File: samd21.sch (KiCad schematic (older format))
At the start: 17 parts, among them IC1 SAMD21G18A, J1 USB_C, J2 DEBUG, SW1 RESET, U4 GD25Q32C

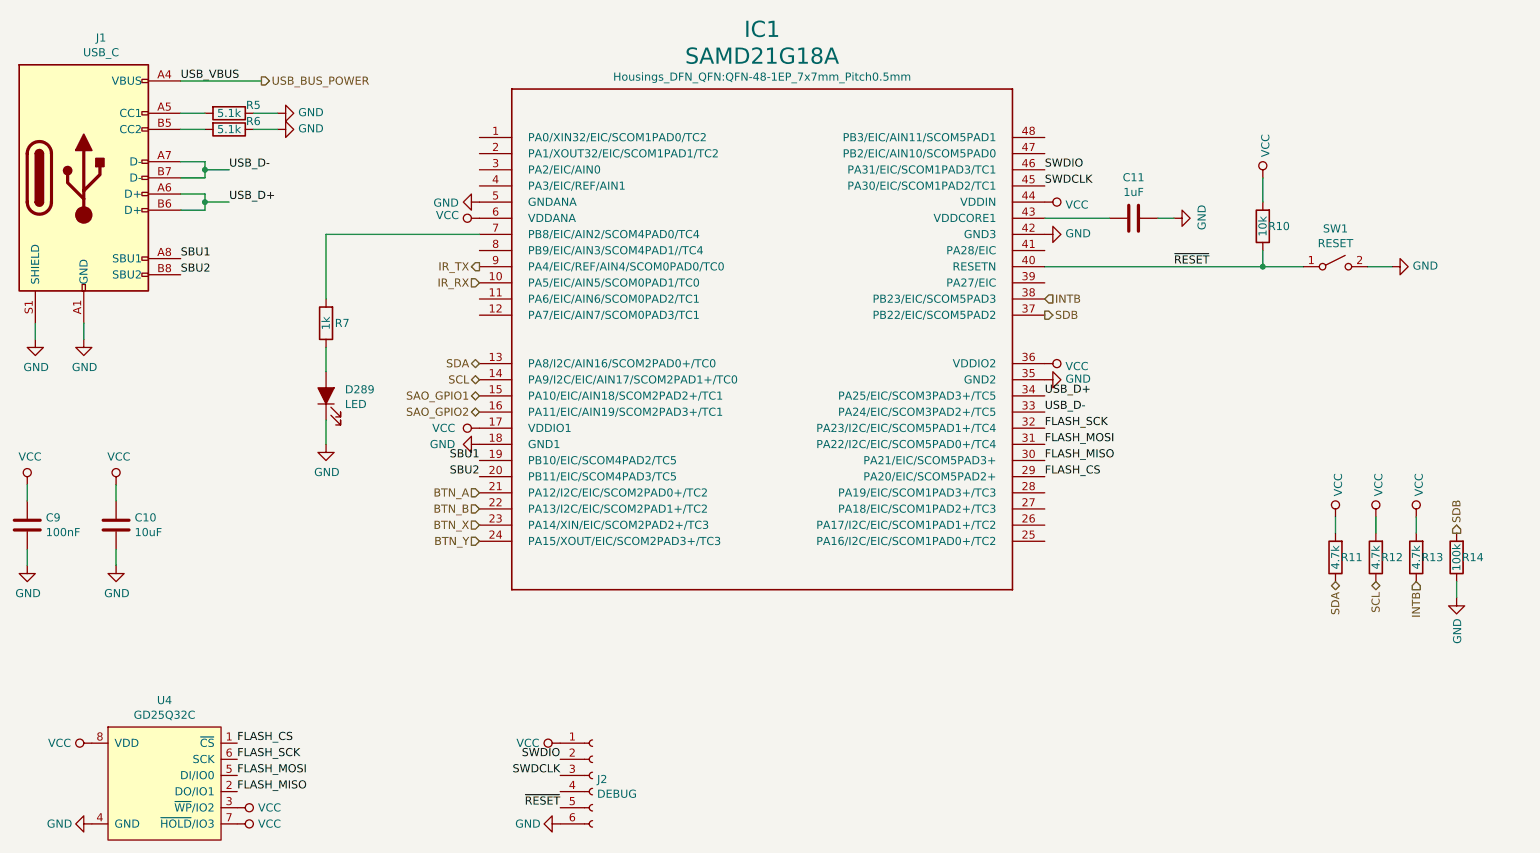
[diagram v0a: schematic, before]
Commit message: Updates to production version
Changed infrared setup, added step-up for battery power, added battery power switch, added more capacitors, changed and added logos, etc.
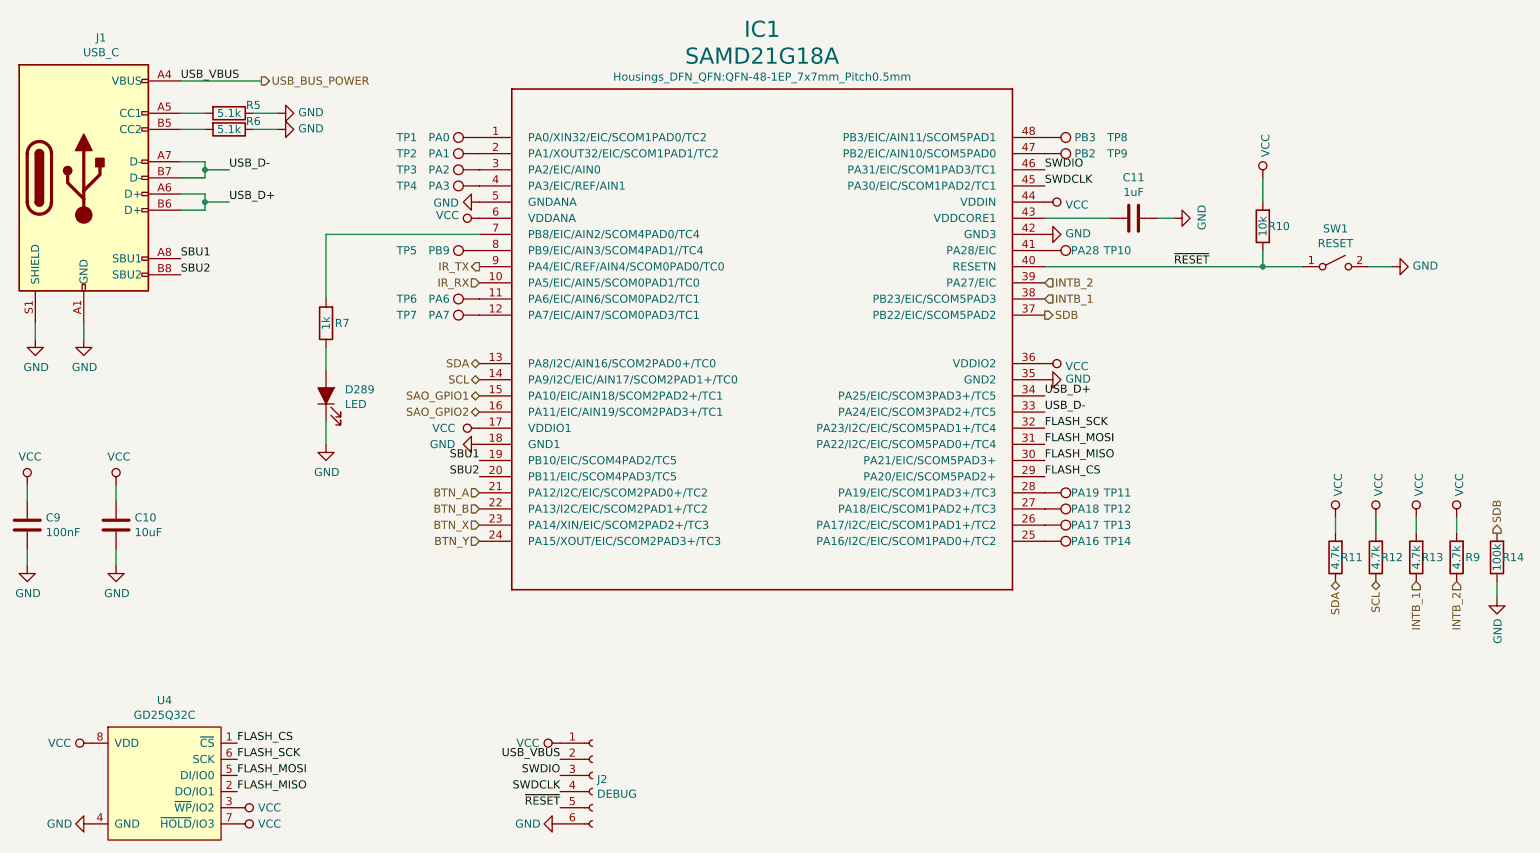
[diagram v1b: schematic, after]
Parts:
- added R9: 4.7k, Resistors_SMD:R_0603, symbol device:R
- added TP1: PA0, Connectors:TestPoint_Large, symbol Connector:TestPoint
- added TP10: PA28, Connectors:TestPoint_Large, symbol Connector:TestPoint
- added TP11: PA19, Connectors:TestPoint_Large, symbol Connector:TestPoint
- added TP12: PA18, Connectors:TestPoint_Large, symbol Connector:TestPoint
- added TP13: PA17, Connectors:TestPoint_Large, symbol Connector:TestPoint
- added TP14: PA16, Connectors:TestPoint_Large, symbol Connector:TestPoint
- added TP2: PA1, Connectors:TestPoint_Large, symbol Connector:TestPoint
- added TP3: PA2, Connectors:TestPoint_Large, symbol Connector:TestPoint
- added TP4: PA3, Connectors:TestPoint_Large, symbol Connector:TestPoint
- added TP5: PB9, Connectors:TestPoint_Large, symbol Connector:TestPoint
- added TP6: PA6, Connectors:TestPoint_Large, symbol Connector:TestPoint
- added TP7: PA7, Connectors:TestPoint_Large, symbol Connector:TestPoint
- added TP8: PB3, Connectors:TestPoint_Large, symbol Connector:TestPoint
- added TP9: PB2, Connectors:TestPoint_Large, symbol Connector:TestPoint
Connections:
- net SWDCLK: now also J2.4 (Pin_4); no longer J2.3 (Pin_3)
- net SWDIO: now also J2.3 (Pin_3); no longer J2.2 (Pin_2)
- net USB_BUS_POWER: now also J2.2 (Pin_2)
- net VCC: now also R9.2
- net at IC1.1 (PA0/XIN32/EIC/SCOM1PAD0/TC2): now also TP1.1
- net at IC1.11 (PA6/EIC/AIN6/SCOM0PAD2/TC1): now also TP6.1
- net at IC1.12 (PA7/EIC/AIN7/SCOM0PAD3/TC1): now also TP7.1
- net at IC1.2 (PA1/XOUT32/EIC/SCOM1PAD1/TC2): now also TP2.1
- net at IC1.25 (PA16/I2C/EIC/SCOM1PAD0+/TC2): now also TP14.1
- net at IC1.26 (PA17/I2C/EIC/SCOM1PAD1+/TC2): now also TP13.1
- net at IC1.27 (PA18/EIC/SCOM1PAD2+/TC3): now also TP12.1
- net at IC1.28 (PA19/EIC/SCOM1PAD3+/TC3): now also TP11.1
- net at IC1.3 (PA2/EIC/AIN0): now also TP3.1
- net INTB_2: now reaches IC1.39 (PA27/EIC)
- net INTB_2: now also R9.1
- net at IC1.4 (PA3/EIC/REF/AIN1): now also TP4.1
- net at IC1.41 (PA28/EIC): now also TP10.1
- net at IC1.47 (PB2/EIC/AIN10/SCOM5PAD0): now also TP9.1
- net at IC1.48 (PB3/EIC/AIN11/SCOM5PAD1): now also TP8.1
- net at IC1.8 (PB9/EIC/AIN3/SCOM4PAD1//TC4): now also TP5.1
- net INTB renamed INTB_1
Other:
- moved on the sheet: R14
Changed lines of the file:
@@
 Text Label 4450 5900 2    50   ~ 0
 ~RESET
-Text Label 4450 5600 2    50   ~ 0
+Text Label 4450 5700 2    50   ~ 0
 SWDIO
-Text Label 4450 5700 2    50   ~ 0
+Text Label 4450 5800 2    50   ~ 0
 SWDCLK
 Text HLabel 3950 3150 0    50   BiDi ~ 0
@@
 $EndComp
 $Comp
-L power:VCC #PWR?
+L power:VCC #PWR067
 U 1 1 5EEE4255
 P 9250 4100
-F 0 "#PWR?" H 9250 3950 50  0001 C CNN
+F 0 "#PWR067" H 9250 3950 50  0001 C CNN
 F 1 "VCC" V 9267 4228 50  0000 L CNN
 F 2 "" H 9250 4100 50  0001 C CNN
@@
 $EndComp
 $Comp
-L power:VCC #PWR?
+L power:VCC #PWR068
 U 1 1 5EEE4871
 P 9500 4100
-F 0 "#PWR?" H 9500 3950 50  0001 C CNN
+F 0 "#PWR068" H 9500 3950 50  0001 C CNN
 F 1 "VCC" V 9517 4228 50  0000 L CNN
 F 2 "" H 9500 4100 50  0001 C CNN
@@
 $EndComp
 $Comp
-L power:VCC #PWR?
+L power:VCC #PWR069
 U 1 1 5EEE49E0
 P 9750 4100
-F 0 "#PWR?" H 9750 3950 50  0001 C CNN
+F 0 "#PWR069" H 9750 3950 50  0001 C CNN
 F 1 "VCC" V 9767 4228 50  0000 L CNN
 F 2 "" H 9750 4100 50  0001 C CNN
@@
 SCL
 Text HLabel 7450 2750 2    50   Input ~ 0
-INTB
-Text HLabel 9750 4500 3    50   Input ~ 0
-INTB
+INTB_1
 Text HLabel 7450 2850 2    50   Output ~ 0
 SDB
@@
 L device:R R14
 U 1 1 5EEEA025
+P 10250 4350
+F 0 "R14" H 10150 4350 50  0000 C CNN
+F 1 "100k" V 10250 4350 50  0000 C CNN
+F 2 "Resistors_SMD:R_0603" V 10180 4350 50  0001 C CNN
+F 3 "~" H 10250 4350 50  0001 C CNN
+	1    10250 4350
+	-1   0    0    1
+$EndComp
+Text HLabel 10250 4200 1    50   Output ~ 0
+SDB
+$Comp
+L power:GND #PWR071
+U 1 1 5EEEA48A
+P 10250 4600
+F 0 "#PWR071" H 10250 4350 50  0001 C CNN
+F 1 "GND" V 10255 4472 50  0000 R CNN
+F 2 "" H 10250 4600 50  0001 C CNN
+F 3 "" H 10250 4600 50  0001 C CNN
+	1    10250 4600
+	1    0    0    -1
+$EndComp
+Wire Wire Line
+	10250 4500 10250 4600
+$Comp
+L Connector:TestPoint TP1
+U 1 1 5F12438C
+P 3950 1750
+F 0 "TP1" V 3950 2200 50  0000 C CNN
+F 1 "PA0" V 3950 2000 50  0000 C CNN
+F 2 "Connectors:TestPoint_Large" H 4150 1750 50  0001 C CNN
+F 3 "~" H 4150 1750 50  0001 C CNN
+	1    3950 1750
+	0    -1   -1   0
+$EndComp
+$Comp
+L Connector:TestPoint TP2
+U 1 1 5F125D74
+P 3950 1850
+F 0 "TP2" V 3950 2300 50  0000 C CNN
+F 1 "PA1" V 3950 2100 50  0000 C CNN
+F 2 "Connectors:TestPoint_Large" H 4150 1850 50  0001 C CNN
+F 3 "~" H 4150 1850 50  0001 C CNN
+	1    3950 1850
+	0    -1   -1   0
+$EndComp
+$Comp
+L Connector:TestPoint TP3
+U 1 1 5F12663A
+P 3950 1950
+F 0 "TP3" V 3950 2400 50  0000 C CNN
+F 1 "PA2" V 3950 2200 50  0000 C CNN
+F 2 "Connectors:TestPoint_Large" H 4150 1950 50  0001 C CNN
+F 3 "~" H 4150 1950 50  0001 C CNN
+	1    3950 1950
+	0    -1   -1   0
+$EndComp
+$Comp
+L Connector:TestPoint TP4
+U 1 1 5F126A64
+P 3950 2050
+F 0 "TP4" V 3950 2500 50  0000 C CNN
+F 1 "PA3" V 3950 2300 50  0000 C CNN
+F 2 "Connectors:TestPoint_Large" H 4150 2050 50  0001 C CNN
+F 3 "~" H 4150 2050 50  0001 C CNN
+	1    3950 2050
+	0    -1   -1   0
+$EndComp
+$Comp
+L Connector:TestPoint TP5
+U 1 1 5F127893
+P 3950 2450
+F 0 "TP5" V 3950 2900 50  0000 C CNN
+F 1 "PB9" V 3950 2700 50  0000 C CNN
+F 2 "Connectors:TestPoint_Large" H 4150 2450 50  0001 C CNN
+F 3 "~" H 4150 2450 50  0001 C CNN
+	1    3950 2450
+	0    -1   -1   0
+$EndComp
+$Comp
+L Connector:TestPoint TP6
+U 1 1 5F127DA0
+P 3950 2750
+F 0 "TP6" V 3950 3200 50  0000 C CNN
+F 1 "PA6" V 3950 3000 50  0000 C CNN
+F 2 "Connectors:TestPoint_Large" H 4150 2750 50  0001 C CNN
+F 3 "~" H 4150 2750 50  0001 C CNN
+	1    3950 2750
+	0    -1   -1   0
+$EndComp
+$Comp
+L Connector:TestPoint TP7
+U 1 1 5F128145
+P 3950 2850
+F 0 "TP7" V 3950 3300 50  0000 C CNN
+F 1 "PA7" V 3950 3100 50  0000 C CNN
+F 2 "Connectors:TestPoint_Large" H 4150 2850 50  0001 C CNN
+F 3 "~" H 4150 2850 50  0001 C CNN
+	1    3950 2850
+	0    -1   -1   0
+$EndComp
+$Comp
+L Connector:TestPoint TP14
+U 1 1 5F128571
+P 7450 4250
+F 0 "TP14" V 7450 4700 50  0000 C CNN
+F 1 "PA16" V 7450 4500 50  0000 C CNN
+F 2 "Connectors:TestPoint_Large" H 7650 4250 50  0001 C CNN
+F 3 "~" H 7650 4250 50  0001 C CNN
+	1    7450 4250
+	0    1    1    0
+$EndComp
+$Comp
+L Connector:TestPoint TP13
+U 1 1 5F1299EA
+P 7450 4150
+F 0 "TP13" V 7450 4600 50  0000 C CNN
+F 1 "PA17" V 7450 4400 50  0000 C CNN
+F 2 "Connectors:TestPoint_Large" H 7650 4150 50  0001 C CNN
+F 3 "~" H 7650 4150 50  0001 C CNN
+	1    7450 4150
+	0    1    1    0
+$EndComp
+$Comp
+L Connector:TestPoint TP12
+U 1 1 5F12A0AD
+P 7450 4050
+F 0 "TP12" V 7450 4500 50  0000 C CNN
+F 1 "PA18" V 7450 4300 50  0000 C CNN
+F 2 "Connectors:TestPoint_Large" H 7650 4050 50  0001 C CNN
+F 3 "~" H 7650 4050 50  0001 C CNN
+	1    7450 4050
+	0    1    1    0
+$EndComp
+$Comp
+L Connector:TestPoint TP11
+U 1 1 5F12A28A
+P 7450 3950
+F 0 "TP11" V 7450 4400 50  0000 C CNN
+F 1 "PA19" V 7450 4200 50  0000 C CNN
+F 2 "Connectors:TestPoint_Large" H 7650 3950 50  0001 C CNN
+F 3 "~" H 7650 3950 50  0001 C CNN
+	1    7450 3950
+	0    1    1    0
+$EndComp
+$Comp
+L Connector:TestPoint TP10
+U 1 1 5F12ABBF
+P 7450 2450
+F 0 "TP10" V 7450 2900 50  0000 C CNN
+F 1 "PA28" V 7450 2700 50  0000 C CNN
+F 2 "Connectors:TestPoint_Large" H 7650 2450 50  0001 C CNN
+F 3 "~" H 7650 2450 50  0001 C CNN
+	1    7450 2450
+	0    1    1    0
+$EndComp
+$Comp
+L Connector:TestPoint TP9
+U 1 1 5F12ADE8
+P 7450 1850
+F 0 "TP9" V 7450 2300 50  0000 C CNN
+F 1 "PB2" V 7450 2100 50  0000 C CNN
+F 2 "Connectors:TestPoint_Large" H 7650 1850 50  0001 C CNN
+F 3 "~" H 7650 1850 50  0001 C CNN
+	1    7450 1850
+	0    1    1    0
+$EndComp
+$Comp
+L Connector:TestPoint TP8
+U 1 1 5F12B04A
+P 7450 1750
+F 0 "TP8" V 7450 2200 50  0000 C CNN
+F 1 "PB3" V 7450 2000 50  0000 C CNN
+F 2 "Connectors:TestPoint_Large" H 7650 1750 50  0001 C CNN
+F 3 "~" H 7650 1750 50  0001 C CNN
+	1    7450 1750
+	0    1    1    0
+$EndComp
+Text HLabel 7450 2650 2    50   Input ~ 0
+INTB_2
+$Comp
+L device:R R9
+U 1 1 5F12E2F7
 P 10000 4350
-F 0 "R14" H 9900 4350 50  0000 C CNN
-F 1 "100k" V 10000 4350 50  0000 C CNN
+F 0 "R9" H 9900 4350 50  0000 C CNN
+F 1 "4.7k" V 10000 4350 50  0000 C CNN
 F 2 "Resistors_SMD:R_0603" V 9930 4350 50  0001 C CNN
 F 3 "~" H 10000 4350 50  0001 C CNN
@@
 	-1   0    0    1
 $EndComp
-Text HLabel 10000 4200 1    50   Output ~ 0
-SDB
-$Comp
-L power:GND #PWR?
-U 1 1 5EEEA48A
-P 10000 4600
-F 0 "#PWR?" H 10000 4350 50  0001 C CNN
-F 1 "GND" V 10005 4472 50  0000 R CNN
-F 2 "" H 10000 4600 50  0001 C CNN
-F 3 "" H 10000 4600 50  0001 C CNN
-	1    10000 4600
-	1    0    0    -1
-$EndComp
-Wire Wire Line
-	10000 4500 10000 4600
+$Comp
+L power:VCC #PWR070
+U 1 1 5F12E301
+P 10000 4100
+F 0 "#PWR070" H 10000 3950 50  0001 C CNN
+F 1 "VCC" V 10017 4228 50  0000 L CNN
+F 2 "" H 10000 4100 50  0001 C CNN
+F 3 "" H 10000 4100 50  0001 C CNN
+	1    10000 4100
+	1    0    0    -1
+$EndComp
+Wire Wire Line
+	10000 4100 10000 4200
+Text HLabel 9750 4500 3    50   Input ~ 0
+INTB_1
+Text HLabel 10000 4500 3    50   Input ~ 0
+INTB_2
+Text Label 4450 5600 2    50   ~ 0
+USB_VBUS
 $EndSCHEMATC
